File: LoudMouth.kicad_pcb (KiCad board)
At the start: 2 copper layers, 15 parts, among them P101 CONN_01X02, P102 CONN_01X02, P103 CONN_01X02, Q101 Q_NPN_BCE

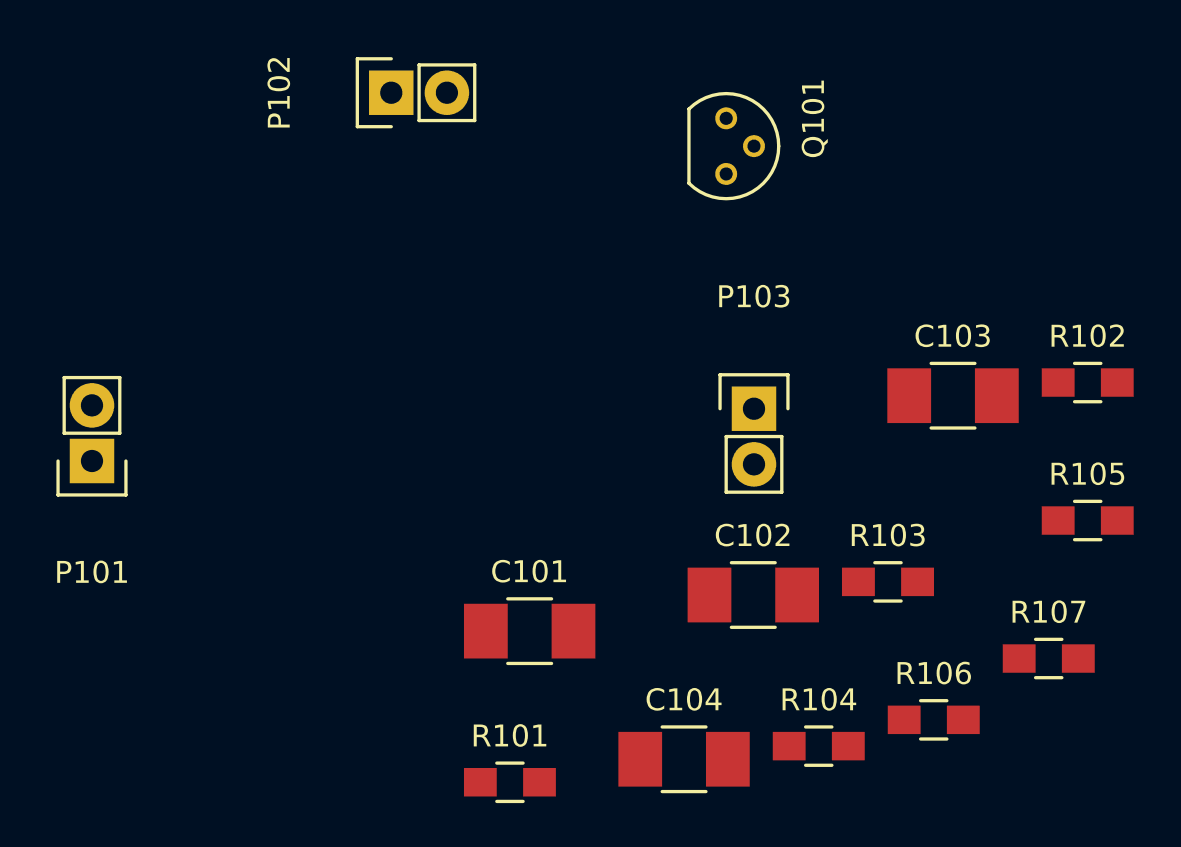
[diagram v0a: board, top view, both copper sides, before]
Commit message: Added all components to footprint
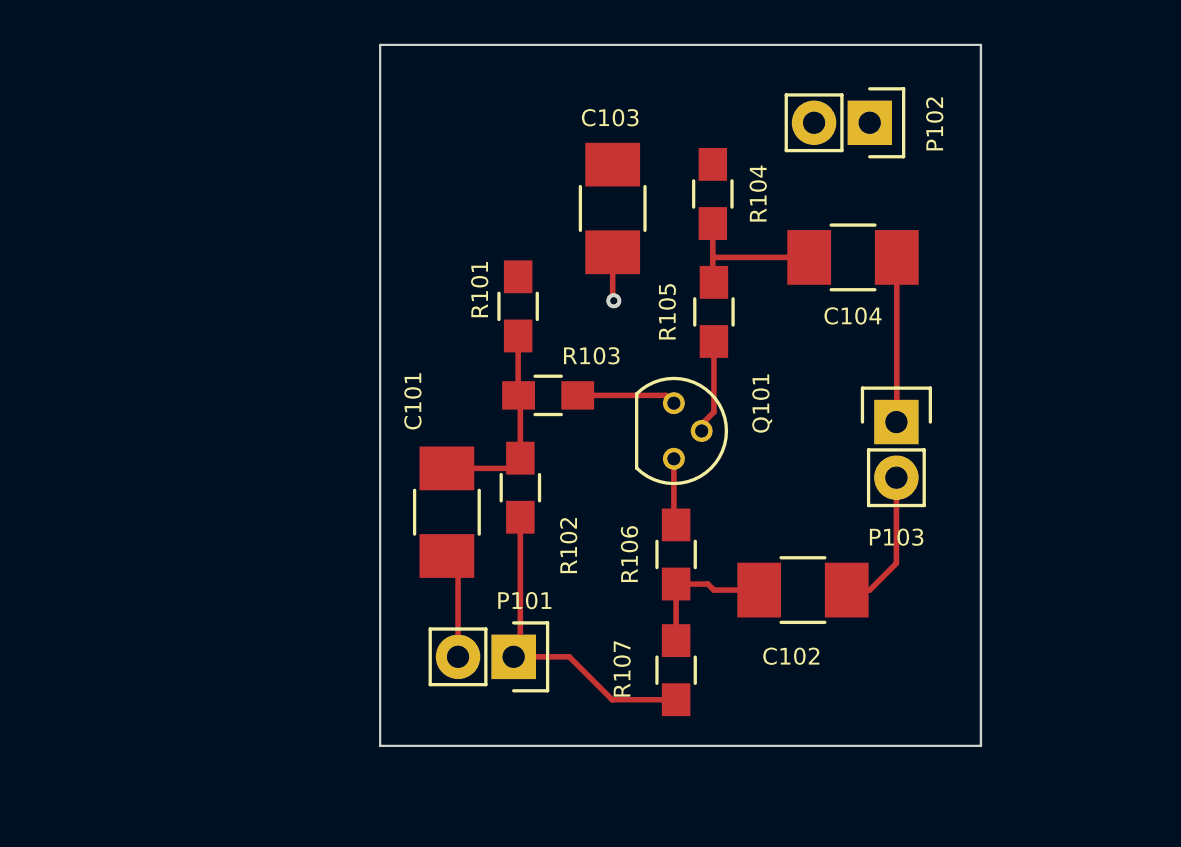
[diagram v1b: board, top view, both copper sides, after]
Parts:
- moved R102 26.3 mm to (162.4, 112.2), turned to 270 degrees
- moved R104 25.7 mm to (171.1, 98.8), turned to 270 degrees
- moved C104 24.2 mm to (177.5, 101.7), turned to 180 degrees
- moved P102 21.9 mm to (178.3, 95.5), turned to 270 degrees
- moved R101 21.7 mm to (162.3, 103.9), turned to 270 degrees
- moved P101 21.2 mm to (162.1, 119.9), turned to 270 degrees
- moved R105 19.5 mm to (171.2, 104.1), turned to 90 degrees
- moved C103 17.7 mm to (166.6, 99.4), turned to 90 degrees
- moved R103 17.7 mm to (163.6, 108.0), turned to 180 degrees
- moved R107 17.0 mm to (169.5, 120.5), turned to 270 degrees
- moved R106 14.0 mm to (169.5, 115.2), turned to 90 degrees
- moved Q101 13.2 mm to (169.4, 108.3)
- moved C101 6.62 mm to (159.0, 113.3), turned to 270 degrees
- moved P103 6.53 mm to (179.5, 109.2)
- moved C102 2.28 mm to (175.3, 116.8), turned to 180 degrees
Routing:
- net GND: track 0.00 -> 23.6 mm, vias 0 -> 1
- net Net-(C101-Pad1): track 0.00 -> 9.17 mm
- net /OUT: track 0.00 -> 7.53 mm
- net Net-(C104-Pad2): track 0.00 -> 7.23 mm
- net Net-(C102-Pad2): track 0.00 -> 6.49 mm
- net /IN: track 0.00 -> 4.81 mm
- net Net-(Q101-Pad1): track 0.00 -> 4.54 mm
- net Net-(Q101-Pad2): track 0.00 -> 4.32 mm
- net Net-(Q101-Pad3): track 0.00 -> 3.06 mm
- added copper zone on F.Cu, net /VCC
- added copper zone on B.Cu, net GND
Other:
- board outline added: 27.4 x 32 mm
- net class Default: clearance 0.2 -> 0.254; trace_width 0.25 -> 0.254; via_dia 0.6 -> 0.6858; via_drill 0.4 -> 0.3302
- rule trace_clearance: 0.2 -> 0.254
- rule trace_min: 0.2 -> 0.1524
- rule via_min_drill: 0.3 -> 0.3302
- rule via_min_size: 0.4 -> 0.6858
